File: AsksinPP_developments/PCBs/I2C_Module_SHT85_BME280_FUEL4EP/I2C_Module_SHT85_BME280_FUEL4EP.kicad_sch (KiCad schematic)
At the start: 14 parts, among them J1 Conn_01x04, J2 Conn_01x04, U1 BME280, U2 SHT85

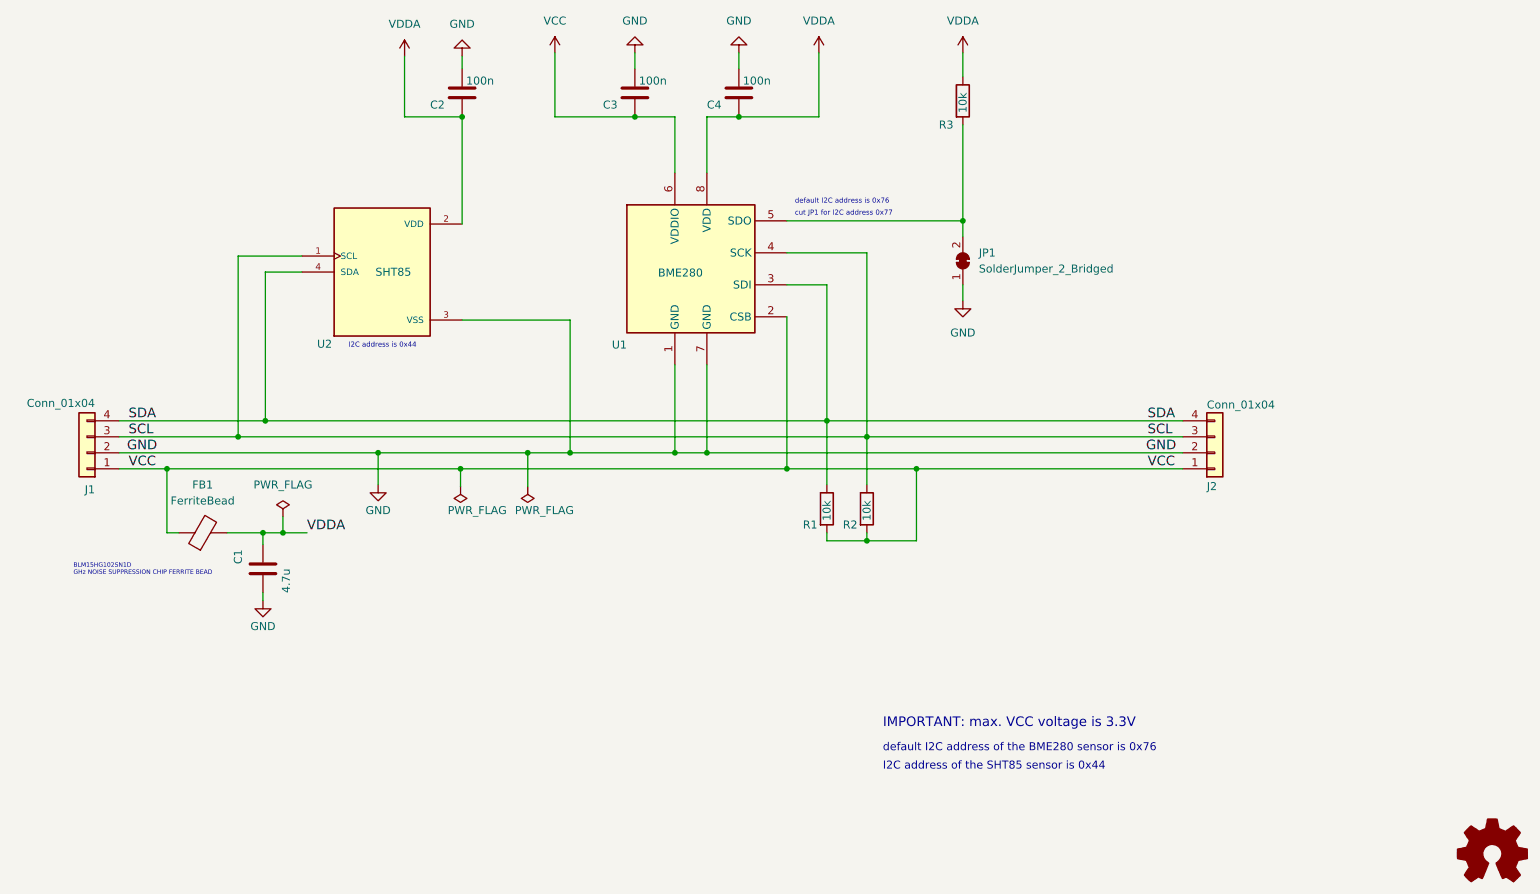
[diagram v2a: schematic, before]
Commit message: PCBs: upgrade some PCBs to KiCAD 7; fix of unnecessary leakage current of I2C address selector: I2C_Module_SHT85_BME280_FUEL4EP, I2C_Module_SHT45_BME280_small_FUEL4EP, I2C_Module_SHT45_BME280_FUEL4EP, I2C_Module_BME280_FUEL4EP, and I2C_Module_BME680_FUEL4EP
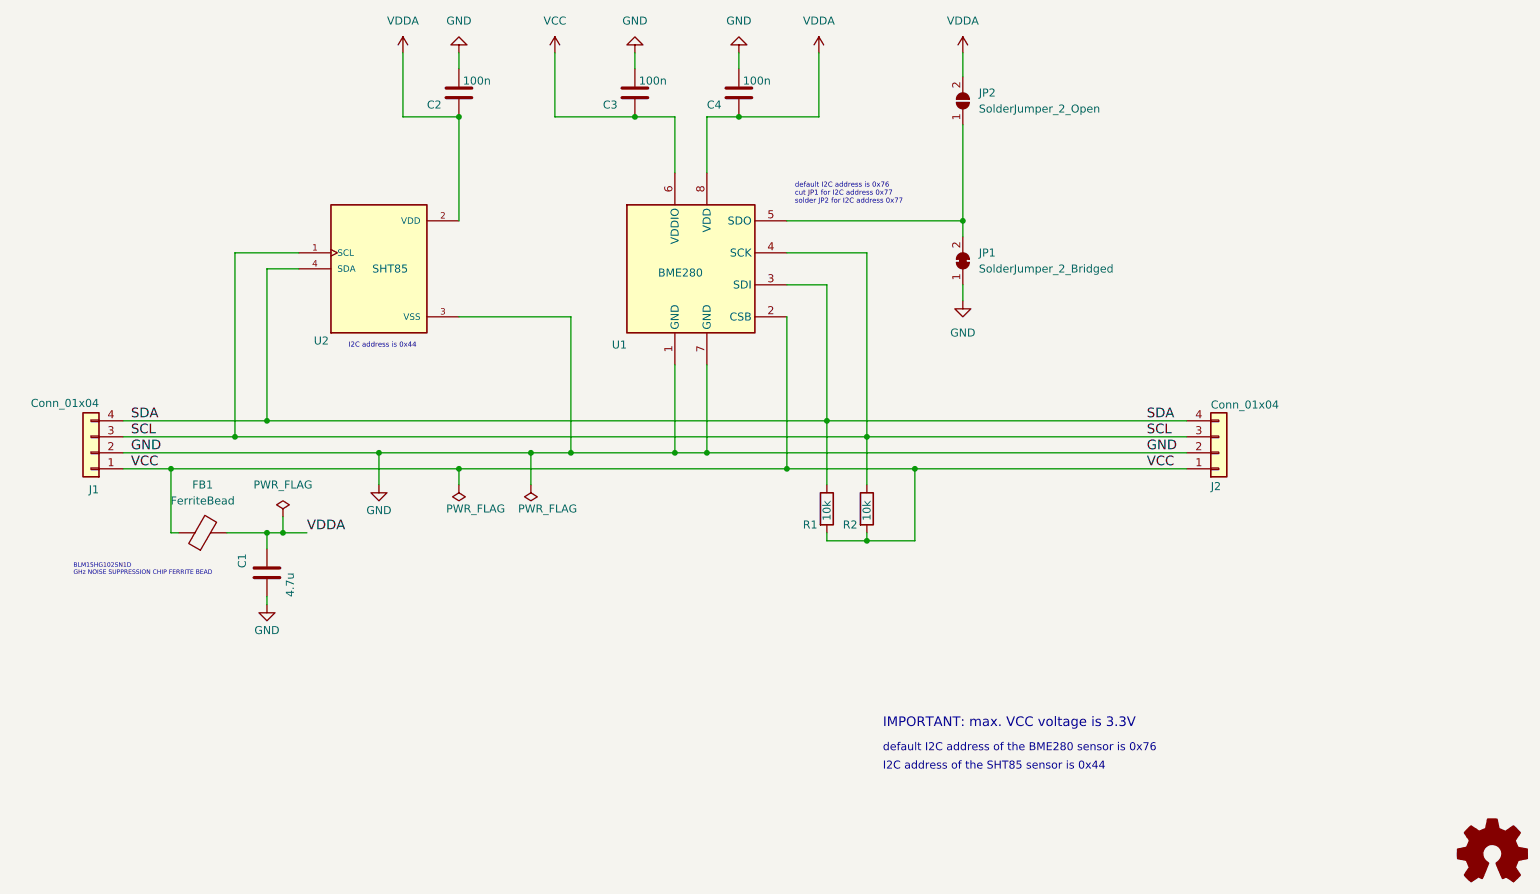
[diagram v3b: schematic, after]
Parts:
- removed R3: 10k, Resistor_SMD:R_0402_1005Metric, symbol Device:R
- added JP2: SolderJumper_2_Open, Jumper:SolderJumper-2_P1.3mm_Open_Pad1.0x1.5mm, symbol Jumper:SolderJumper_2_Open
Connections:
- net VDDA: now also JP2.2 (B)
- net at JP1.2 (B), U1.5 (SDO): now also JP2.1 (A)
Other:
- note added: "solder JP2 for I2C address 0x77"
- moved on the sheet: C1, C2, J1, J2, U2

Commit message: PCBs/I2C_Module_SHT85_BME280: migration to KiCAD 8; fix of DRC rules
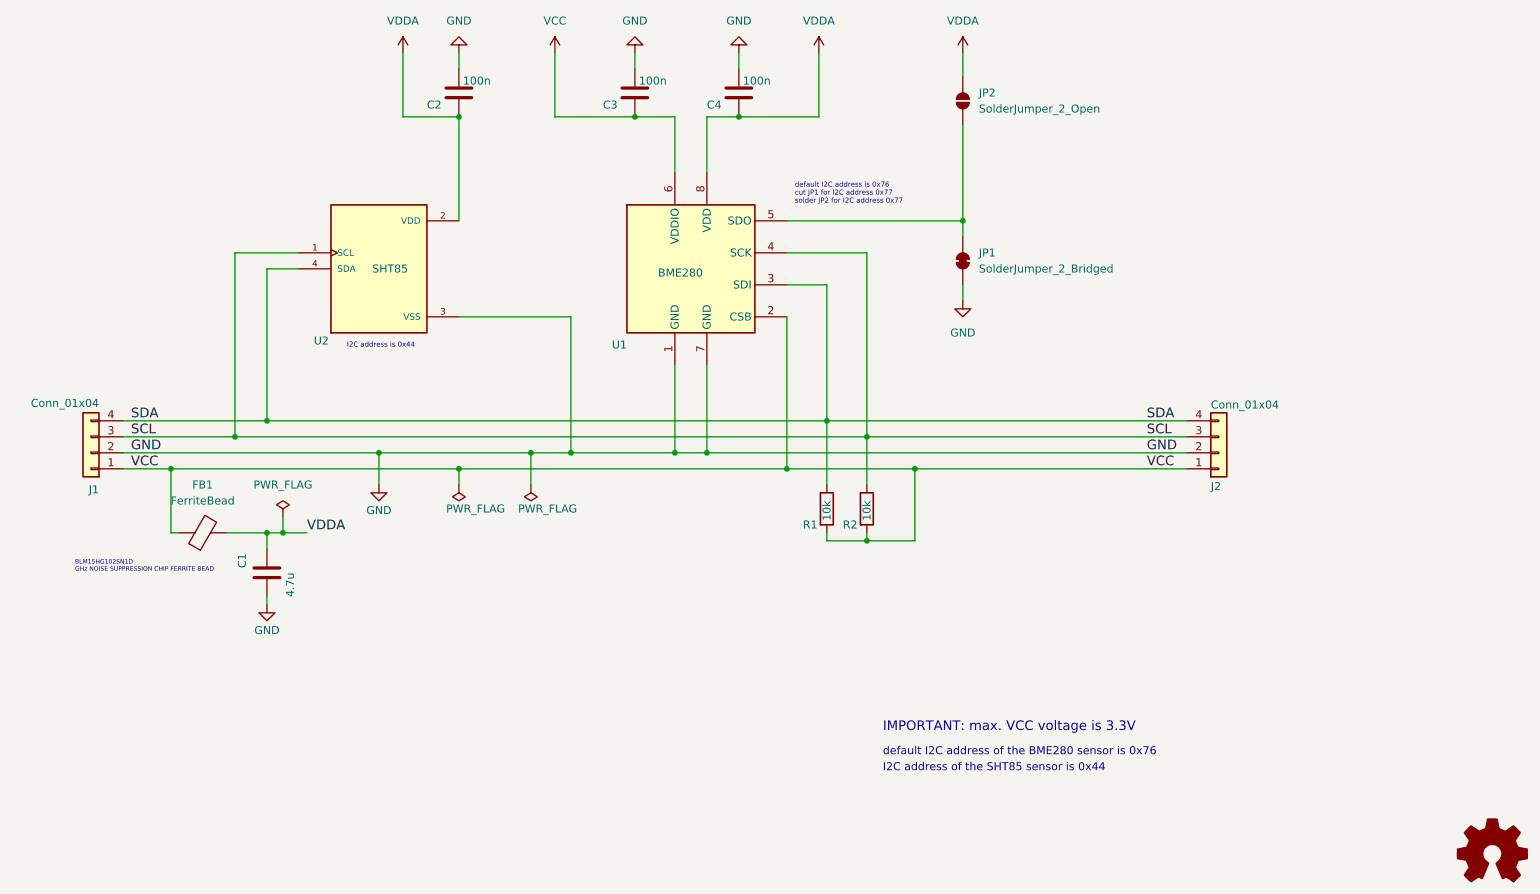
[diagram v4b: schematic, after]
